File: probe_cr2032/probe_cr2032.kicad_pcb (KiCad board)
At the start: 2 copper layers, 28.8 x 28.8 mm, 16 parts, among them U1 MCP73831-2-OT

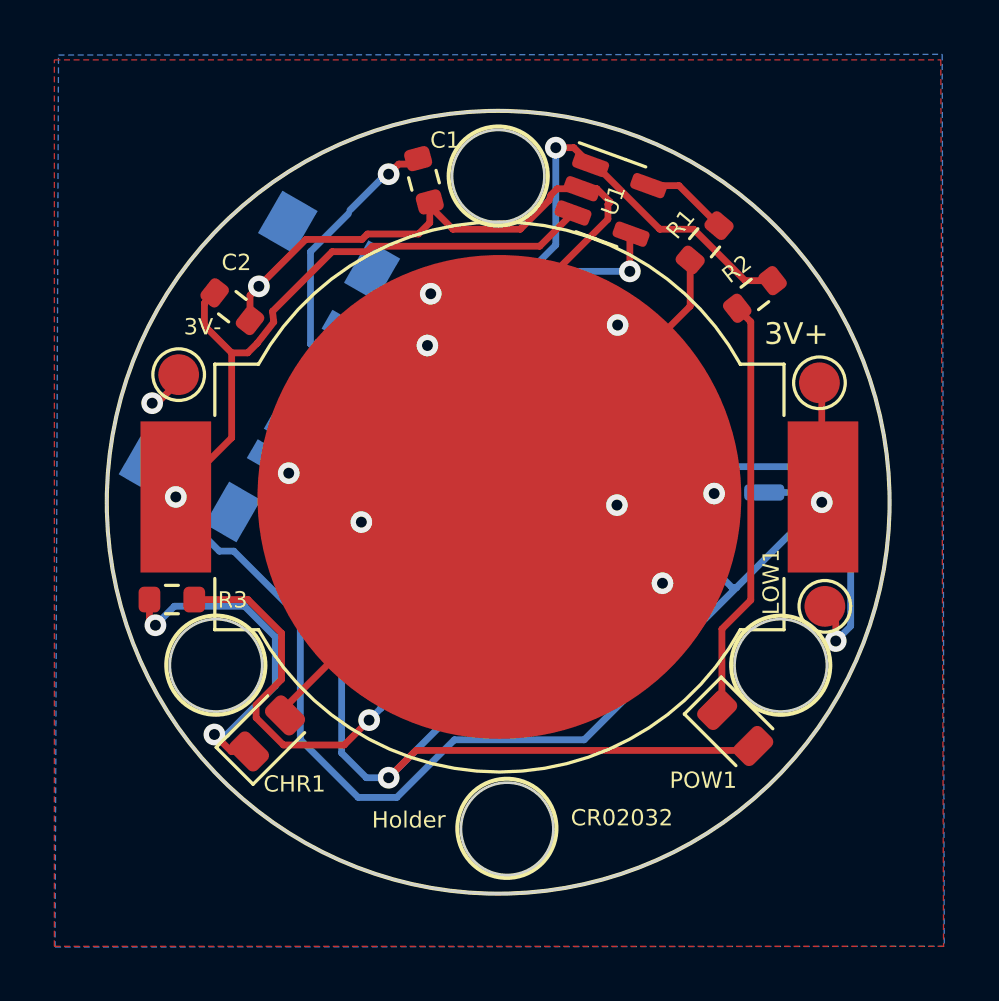
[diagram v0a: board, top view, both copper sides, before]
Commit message: - add new probe_cr_2032
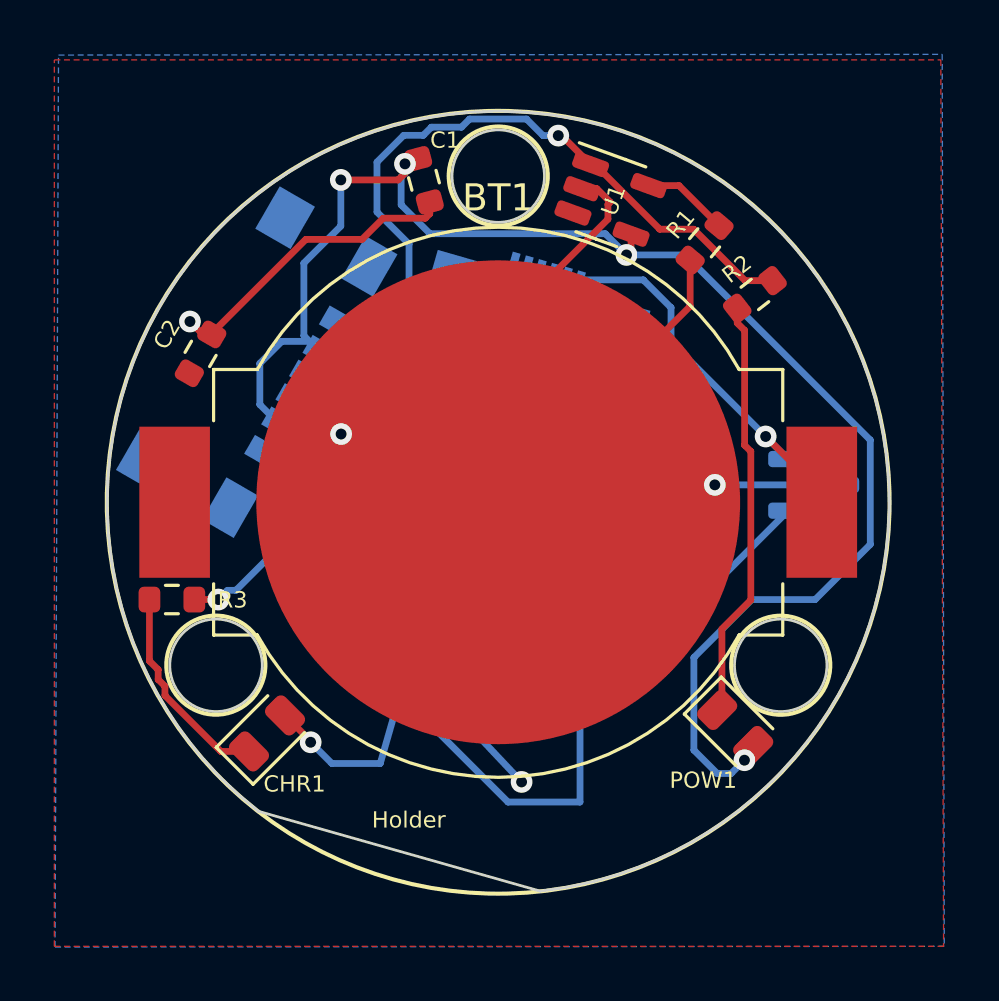
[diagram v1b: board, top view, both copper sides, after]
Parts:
- removed 3V+, 3V-, LOW1: , TestPoint:TestPoint_Pad_D1.5mm
- removed CR02032: BAT, Battery:BatteryHolder_MPD_BC2003_1x2032
- removed J?: Conn_01x03, Connector_Molex:Molex_CLIK-Mate_502386-0370_1x03-1MP_P1.25mm_Horizontal
- removed U?: APX809-23SAG-7, Package_TO_SOT_SMD:SOT-23
- added BT1: Battery, Battery:BatteryHolder_MPD_BC2003_1x2032, F.Cu at (100.0, 100.0)
- added J2: Conn_01x06, Connector_FFC-FPC:TE_0-1734839-6_1x06-1MP_P0.5mm_Horizontal, B.Cu at (101.4, 93.0)
- added J3: Conn_01x06, Connector_FFC-FPC:TE_0-1734839-6_1x06-1MP_P0.5mm_Horizontal, B.Cu at (98.2, 105.1)
- added U2: MCP101-300D, Package_TO_SOT_SMD:SOT-23, B.Cu at (111.6, 99.4)
-  : value Probe Power v1.3 -> Probe Power v1.4
- moved   7.59 mm to (105.4, 101.1)
- moved C2 2.09 mm to (89.0, 94.5), turned to 60 degrees
- moved USBC1 0.19 mm to (90.1, 94.3)
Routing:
- net Net-(BT1-+): track 76.6 -> 35.7 mm
- net Net-(J2-Pin_5): track 0.00 -> 38.1 mm
- net unconnected-(LOW1-Pad1): track 24.4 -> 0.00 mm, vias 1 -> 0
- net Net-(J2-Pin_2): track 0.00 -> 12.6 mm
- net Net-(J2-Pin_3): track 0.00 -> 12.6 mm
- net Net-(J2-Pin_4): track 0.00 -> 12.6 mm
- net Net-(POW1-A): track 68.3 -> 58.4 mm, vias 3 -> 4
- net Net-(U1-STAT): track 46.1 -> 38.5 mm
- net GND: track 72.6 -> 67.7 mm, vias 10 -> 4
- net Net-(CHR1-K): track 12.7 -> 8.00 mm, vias 2 -> 0
- added copper zone on F.Cu, net Net-(BT1-+)
- removed copper zone on F.Cu, net Net-(POW1-A)
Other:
- board size 28.8 x 28.8 mm -> 28.8 x 28.7 mm

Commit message: -prepare for production
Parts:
- removed  : Probe Power v1.4, LOGO
- R1, R2, U1: moved to B.Cu
- moved R1 23.1 mm to (97.4, 111.2), turned to -90 degrees
- moved U1 22.7 mm to (100.1, 111.1), turned to -90 degrees
- moved R2 19.9 mm to (102.8, 111.1), turned to 90 degrees
- moved J2 3.17 mm to (102.5, 95.9), turned to -30 degrees
- moved J3 0.82 mm to (97.7, 104.5), turned to -30 degrees
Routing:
- net Net-(U1-STAT): track 38.5 -> 18.8 mm, vias 2 -> 1
- net GND: track 67.7 -> 48.4 mm, vias 4 -> 5
- net Net-(BT1-+): track 35.7 -> 51.2 mm, vias 2 -> 1
- net Net-(POW1-A): track 58.4 -> 67.3 mm
- net Net-(POW1-K): track 15.3 -> 8.11 mm, vias 0 -> 1
- net Net-(J2-Pin_5): track 38.1 -> 31.3 mm
- net Net-(J2-Pin_2): track 12.6 -> 9.83 mm
- net Net-(J2-Pin_3): track 12.6 -> 9.83 mm
- net Net-(J2-Pin_4): track 12.6 -> 9.83 mm
- net Net-(U1-PROG): track 3.20 -> 1.83 mm
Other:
- board size 28.8 x 28.7 mm -> 28.8 x 28.8 mm
- board text removed: "Holder"

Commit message: -add last fix for attinty84
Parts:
- turned CHR1 to -135 degrees
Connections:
- CHR1 pad 1: Net-(CHR1-K) -> GND
- CHR1 pad 2: GND -> Net-(CHR1-A)
- R3 pad 2: Net-(CHR1-K) -> Net-(CHR1-A)
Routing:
- net Net-(CHR1-K): track 8.00 -> 0.00 mm
- net Net-(CHR1-A): track 0.00 -> 8.00 mm
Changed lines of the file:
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@@
 	(net 1 "GND")
 	(net 2 "Net-(POW1-A)")
-	(net 3 "Net-(CHR1-K)")
+	(net 3 "Net-(CHR1-A)")
 	(net 4 "Net-(J2-Pin_4)")
 	(net 5 "Net-(J2-Pin_3)")
@@
 			(layers "F.Cu" "F.Mask" "F.Paste")
 			(roundrect_rratio 0.25)
-			(net 3 "Net-(CHR1-K)")
+			(net 3 "Net-(CHR1-A)")
 			(pintype "passive")
 		)
@@
 	(footprint "LED_SMD:LED_0805_2012Metric"
 		(layer "F.Cu")
-		(at 91.494 108.5044 45)
+		(at 91.494 108.5044 -135)
 		(descr "LED SMD 0805 (2012 Metric), square (rectangular) end terminal, IPC_7351 nominal, (Body size source: https://docs.google.com/spreadsheets/d/1BsfQQcO9C6DZCsRaXUlFlo91Tg2WpOkGARC1WS5S8t0/edit?usp=sharing), generated with kicad-footprint-generator")
 		(tags "LED")
 		(property "Reference" "CHR1"
-			(at -0.600457 2.032932 0)
+			(at 0.890672 -2.115381 0)
 			(layer "F.SilkS")
 			(effects
@@
 		(attr smd)
 		(fp_line
+			(start 1 -0.96)
+			(end -1.684999 -0.96)
+			(stroke
+				(width 0.12)
+				(type solid)
+			)
+			(layer "F.SilkS")
+		)
+		(fp_line
+			(start -1.684999 0.96)
+			(end 1 0.96)
+			(stroke
+				(width 0.12)
+				(type solid)
+			)
+			(layer "F.SilkS")
+		)
+		(fp_line
 			(start -1.684999 -0.96)
 			(end -1.684999 0.96)
@@
 		)
 		(fp_line
-			(start -1.684999 0.96)
-			(end 1 0.96)
-			(stroke
-				(width 0.12)
-				(type solid)
-			)
-			(layer "F.SilkS")
-		)
-		(fp_line
-			(start 1 -0.96)
-			(end -1.684999 -0.96)
-			(stroke
-				(width 0.12)
-				(type solid)
-			)
-			(layer "F.SilkS")
+			(start 1.68 0.95)
+			(end -1.68 0.95)
+			(stroke
+				(width 0.05)
+				(type solid)
+			)
+			(layer "F.CrtYd")
+		)
+		(fp_line
+			(start 1.68 -0.95)
+			(end 1.68 0.95)
+			(stroke
+				(width 0.05)
+				(type solid)
+			)
+			(layer "F.CrtYd")
+		)
+		(fp_line
+			(start -1.68 0.95)
+			(end -1.68 -0.95)
+			(stroke
+				(width 0.05)
+				(type solid)
+			)
+			(layer "F.CrtYd")
 		)
 		(fp_line
@@
 		)
 		(fp_line
-			(start -1.68 0.95)
-			(end -1.68 -0.95)
-			(stroke
-				(width 0.05)
-				(type solid)
-			)
-			(layer "F.CrtYd")
-		)
-		(fp_line
-			(start 1.68 -0.95)
-			(end 1.68 0.95)
-			(stroke
-				(width 0.05)
-				(type solid)
-			)
-			(layer "F.CrtYd")
-		)
-		(fp_line
-			(start 1.68 0.95)
-			(end -1.68 0.95)
-			(stroke
-				(width 0.05)
-				(type solid)
-			)
-			(layer "F.CrtYd")
+			(start 1 0.6)
+			(end 1 -0.6)
+			(stroke
+				(width 0.1)
+				(type solid)
+			)
+			(layer "F.Fab")
+		)
+		(fp_line
+			(start 1 -0.6)
+			(end -0.7 -0.6)
+			(stroke
+				(width 0.1)
+				(type solid)
+			)
+			(layer "F.Fab")
+		)
+		(fp_line
+			(start -1 0.6)
+			(end 1 0.6)
+			(stroke
+				(width 0.1)
+				(type solid)
+			)
+			(layer "F.Fab")
+		)
+		(fp_line
+			(start -1 -0.3)
+			(end -1 0.6)
+			(stroke
+				(width 0.1)
+				(type solid)
+			)
+			(layer "F.Fab")
 		)
 		(fp_line
@@
 			(layer "F.Fab")
 		)
-		(fp_line
-			(start -1 -0.3)
-			(end -1 0.6)
-			(stroke
-				(width 0.1)
-				(type solid)
-			)
-			(layer "F.Fab")
-		)
-		(fp_line
-			(start -1 0.6)
-			(end 1 0.6)
-			(stroke
-				(width 0.1)
-				(type solid)
-			)
-			(layer "F.Fab")
-		)
-		(fp_line
-			(start 1 -0.6)
-			(end -0.7 -0.6)
-			(stroke
-				(width 0.1)
-				(type solid)
-			)
-			(layer "F.Fab")
-		)
-		(fp_line
-			(start 1 0.6)
-			(end 1 -0.6)
-			(stroke
-				(width 0.1)
-				(type solid)
-			)
-			(layer "F.Fab")
-		)
 		(fp_text user "${REFERENCE}"
 			(at 0 0 45)
@@
 		)
 		(pad "1" smd roundrect
-			(at -0.937501 0 45)
-			(size 0.975 1.4)
-			(layers "F.Cu" "F.Mask" "F.Paste")
-			(roundrect_rratio 0.25)
-			(net 3 "Net-(CHR1-K)")
-			(pinfunction "K")
-			(pintype "passive")
-		)
-		(pad "2" smd roundrect
-			(at 0.937501 0 45)
+			(at -0.937501 0 225)
 			(size 0.975 1.4)
 			(layers "F.Cu" "F.Mask" "F.Paste")
 			(roundrect_rratio 0.25)
 			(net 1 "GND")
+			(pinfunction "K")
+			(pintype "passive")
+		)
+		(pad "2" smd roundrect
+			(at 0.937501 0 225)
+			(size 0.975 1.4)
+			(layers "F.Cu" "F.Mask" "F.Paste")
+			(roundrect_rratio 0.25)
+			(net 3 "Net-(CHR1-A)")
 			(pinfunction "A")
 			(pintype "passive")
